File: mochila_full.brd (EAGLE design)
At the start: 100 x 80 mm, 13 parts, among them IC1 AD620R

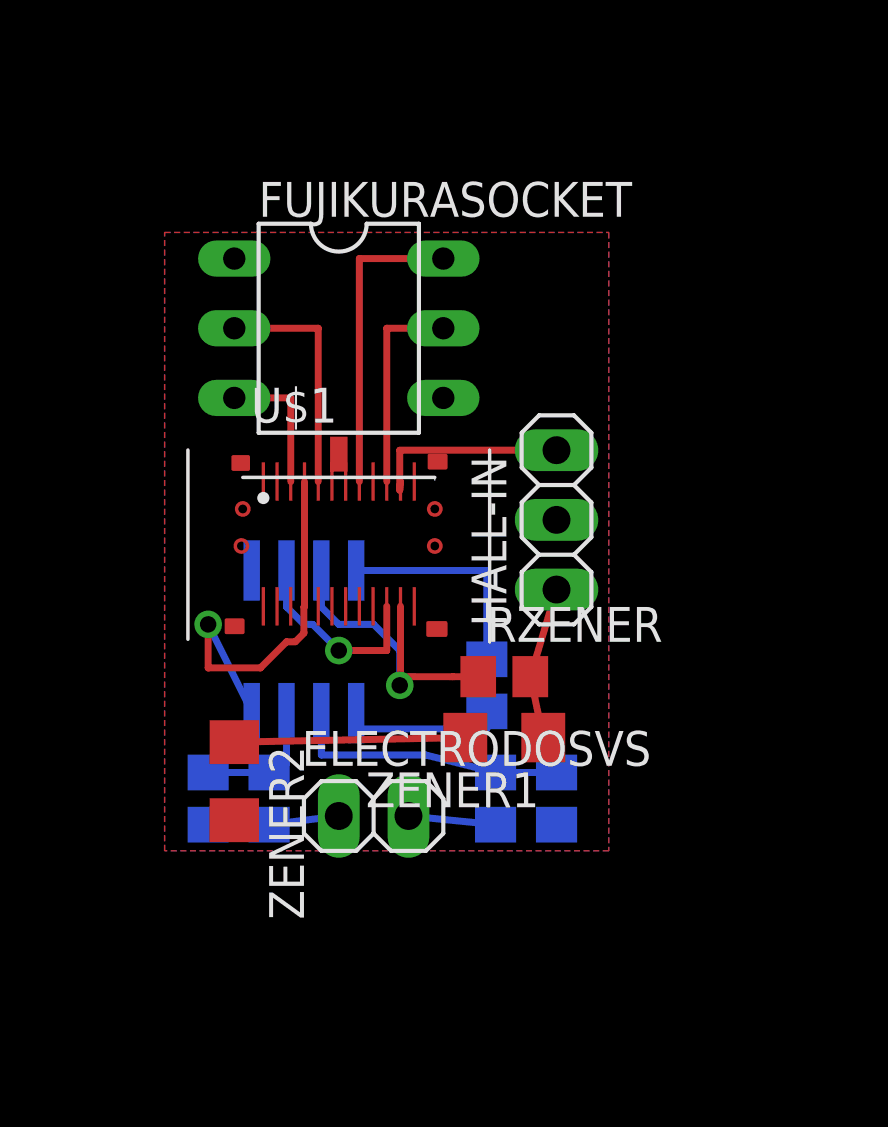
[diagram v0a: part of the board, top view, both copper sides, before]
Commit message: Corregimos placa de conexion universal y mochila
Esta version se envia a imprimir
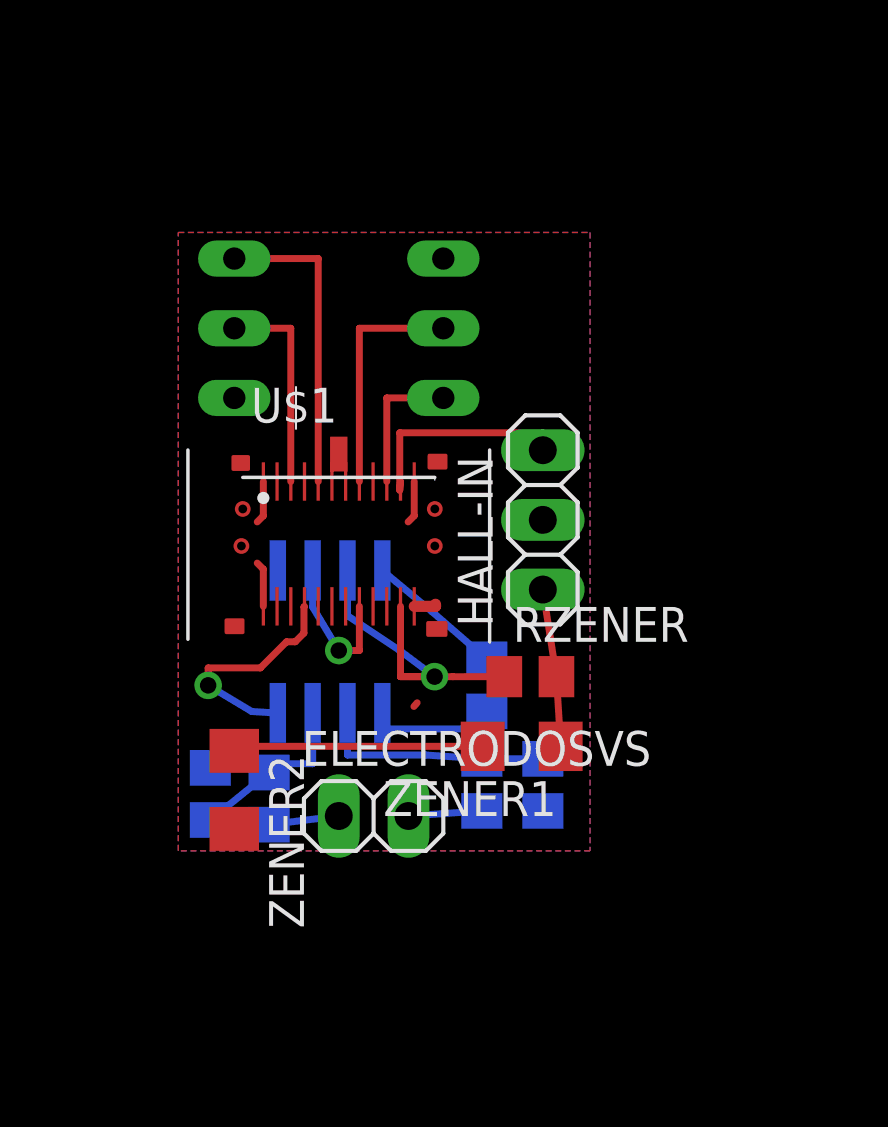
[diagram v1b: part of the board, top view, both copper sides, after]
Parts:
- moved IC1 0.95 mm to (33.7, 24.1)
- moved RZENER 0.95 mm to (41.0, 22.9)
- moved ZENER1 0.71 mm to (40.6, 20.3)
- moved CF1 0.71 mm to (39.2, 18.9)
- moved RF1 0.71 mm to (41.4, 18.9)
- moved HALL-IN 0.50 mm to (41.4, 28.6)
- moved ZENER2 0.32 mm to (30.2, 18.7)
- moved RF2 0.19 mm to (29.3, 18.6), turned to 270 degrees
- flipped FUJIKURASOCKET to the bottom
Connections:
- removed net NC4: U$1.B5
- removed net NC5: U$1.P+
- new net NC6: U$1.B3
- new net NC7: U$1.B8
- net +I: now also FUJIKURASOCKET.2, U$1.-I; no longer FUJIKURASOCKET.5, U$1.HALL
- net -I: now also FUJIKURASOCKET.5, U$1.+12V; no longer FUJIKURASOCKET.2, U$1.+I
- net EXTRA1: now also U$1.P+; no longer U$1.B8
- net OUTP+: now also FUJIKURASOCKET.3, U$1.HALL; no longer FUJIKURASOCKET.6, U$1.-I
- net OUTP-: now also FUJIKURASOCKET.6, U$1.+I; no longer FUJIKURASOCKET.3, U$1.+12V
- net OUTT: now also U$1.B5; no longer U$1.B3
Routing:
- net -12V: track 14.7 -> 8.44 mm
- net OUTP-: track 5.11 -> 11.2 mm
- net OUTP+: track 11.2 -> 5.11 mm
- net GND: track 0.00 -> 5.84 mm
- net N$6: track 8.00 -> 5.00 mm
- net OUTT: track 7.25 -> 5.54 mm
- net N$4: track 10.2 -> 8.65 mm
- net N$2: track 4.78 -> 6.26 mm
- net +12V: track 11.8 -> 13.1 mm
- net -I: track 8.65 -> 7.65 mm
- net +I: track 7.65 -> 8.65 mm
- net N$5: track 5.98 -> 5.02 mm
- net N$8: track 8.42 -> 9.22 mm
- net N$3: track 3.19 -> 2.68 mm

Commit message: Con nueva version de la libreria
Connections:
- net +12V: now also U$1.+12V; no longer U$1.B2
- net +I: now also U$1.+I; no longer U$1.-I
- net -12V: now also U$1.-12VA, U$1.-12VB; no longer U$1.T1, U$1.T4
- net -I: now also U$1.-I; no longer U$1.+12V
- net EXTRA1: now also U$1.E1; no longer U$1.P+
- net EXTRA2: now also U$1.E2; no longer U$1.P-
- net N$24: now also U$1.NC6; no longer U$1.B7
- net N$25: now also U$1.NC5; no longer U$1.B6
- net NC1: now also U$1.NC1; no longer U$1.-12V
- net NC2: now also U$1.NC2; no longer U$1.T2
- net NC3: now also U$1.NC4; no longer U$1.T3
- net NC6: now also U$1.NC3; no longer U$1.B3
- net NC7: now also U$1.NC7; no longer U$1.B8
- net OUTH: now also U$1.HALL; no longer U$1.01
- net OUTP+: now also U$1.P+; no longer U$1.HALL
- net OUTP-: now also U$1.P-; no longer U$1.+I
- net OUTT: now also U$1.T; no longer U$1.B5
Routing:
- net GND: track 5.84 -> 2.71 mm

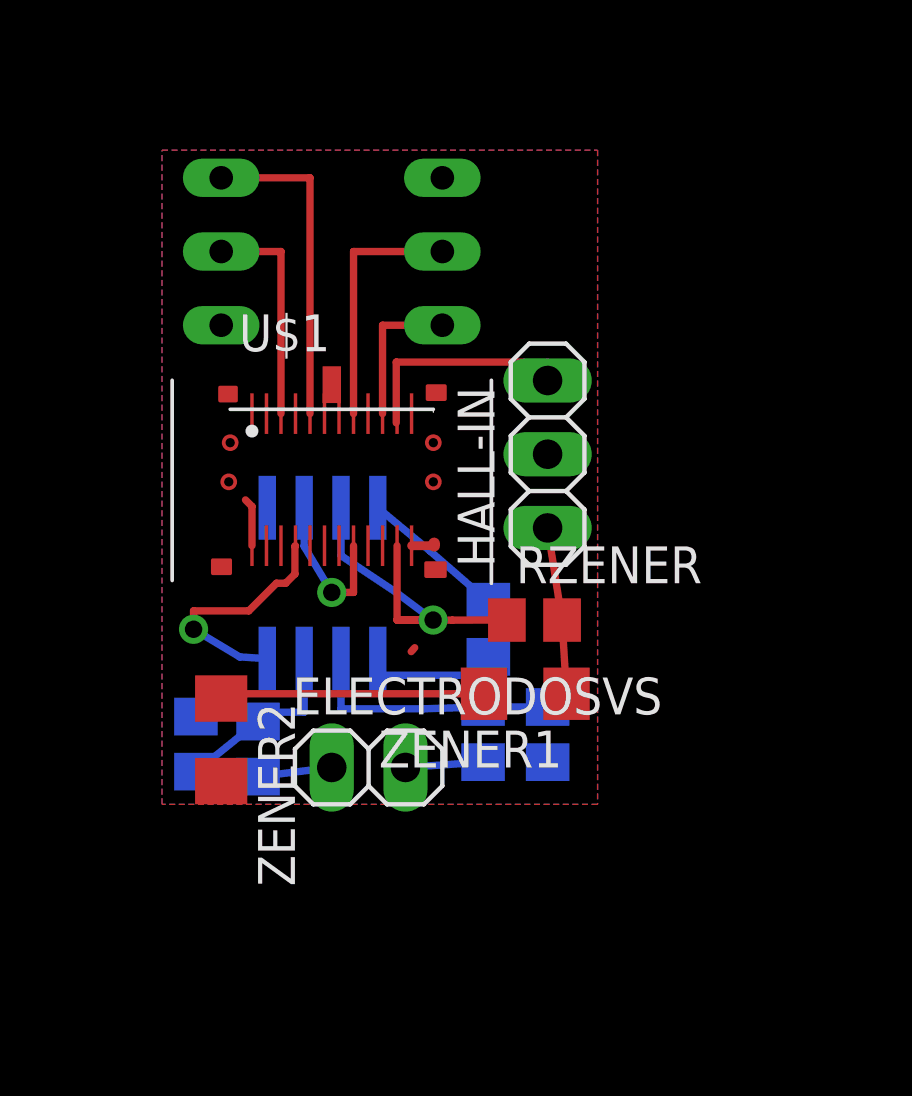
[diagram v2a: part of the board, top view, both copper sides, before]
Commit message: Cambios minimos caja, update libreria conector para mochila
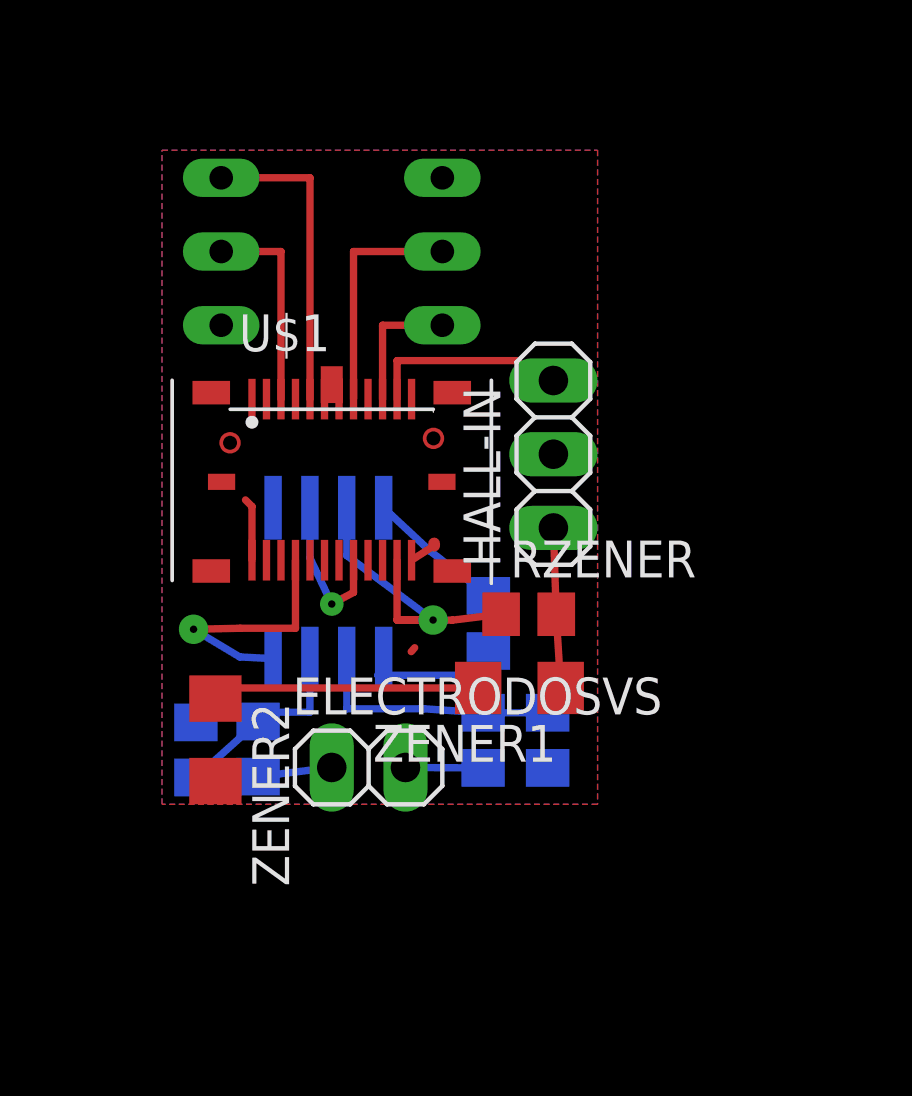
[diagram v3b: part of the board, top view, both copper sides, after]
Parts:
- moved RZENER 0.28 mm to (40.8, 23.1)
- moved ZENER1 0.28 mm to (40.4, 20.5)
- moved HALL-IN 0.20 mm to (41.6, 28.6)
- moved ZENER2 0.20 mm to (30.0, 18.7)
- moved CF1 0.20 mm to (39.2, 18.7)
- moved RF1 0.20 mm to (41.4, 18.7)
- moved RF2 0.20 mm to (29.3, 18.4)
- moved RG 0.20 mm to (39.4, 22.7)
- moved IC1 0.20 mm to (33.9, 24.1)
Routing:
- net +12V: track 13.1 -> 12.3 mm
- net GND: track 2.71 -> 3.35 mm
- net OUTH: track 7.94 -> 7.40 mm
- net OUTP-: track 11.2 -> 10.7 mm
- net OUTP+: track 5.11 -> 4.61 mm
- net -I: track 7.65 -> 7.15 mm
- net +I: track 8.65 -> 8.15 mm

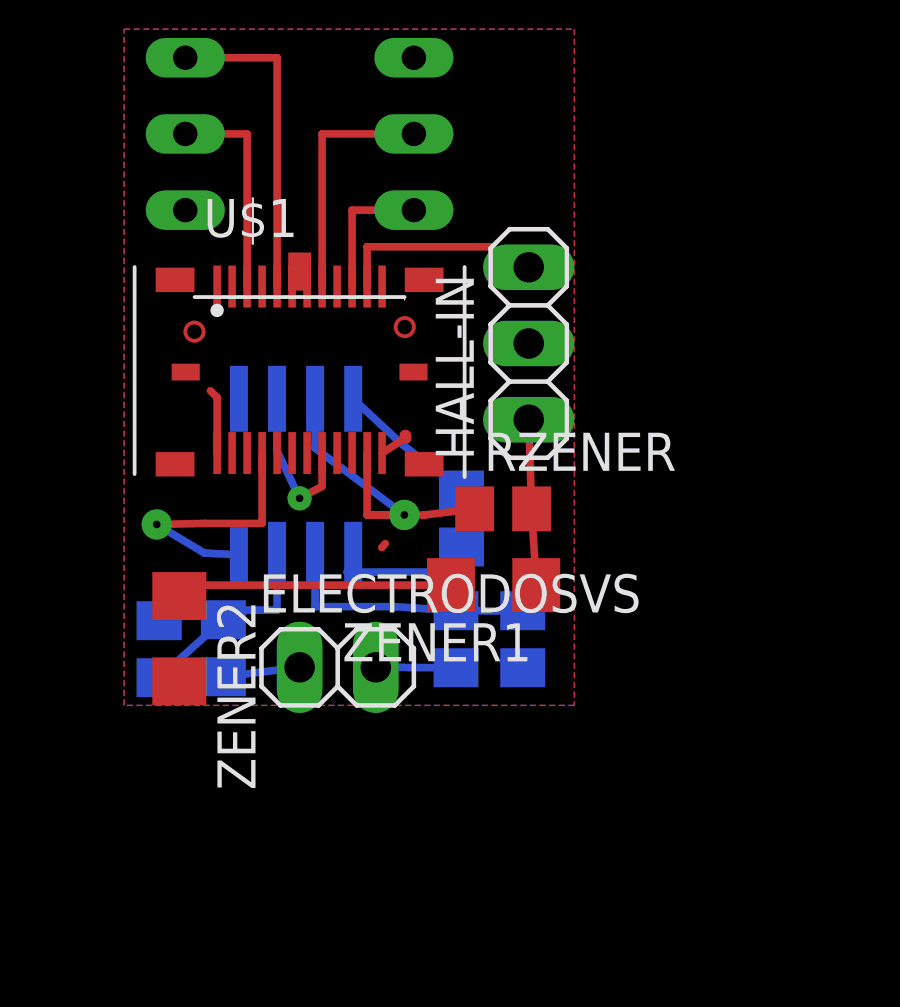
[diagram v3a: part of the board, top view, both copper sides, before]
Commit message: Modifico posicion de R3 y de la pista que lo une con el OPAM. Antes la pista pasaba debajo de un agujero para que pase el sostenedor del conector USBC.
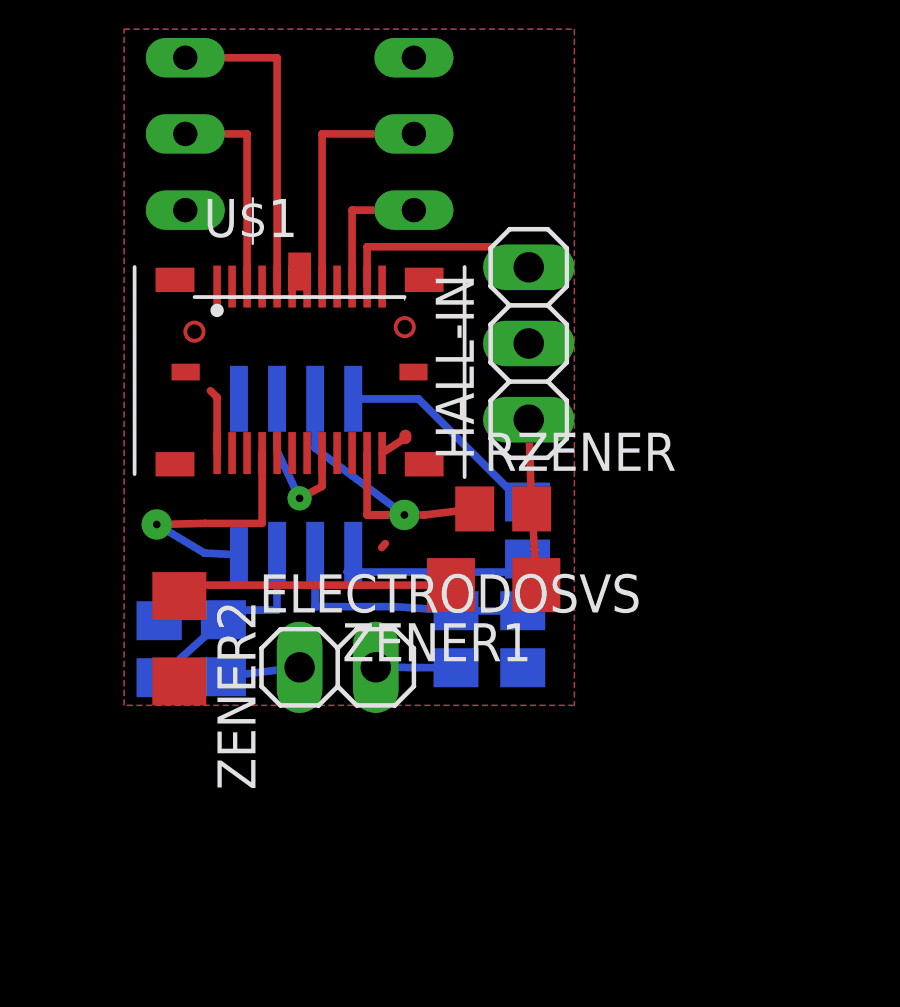
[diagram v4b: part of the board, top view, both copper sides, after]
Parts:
- moved RG 2.24 mm to (41.6, 22.3)
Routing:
- net N$6: track 4.72 -> 7.23 mm
- net N$5: track 5.26 -> 7.06 mm
